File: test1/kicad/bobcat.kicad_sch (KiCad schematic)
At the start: 24 parts, among them U20 Bobcat

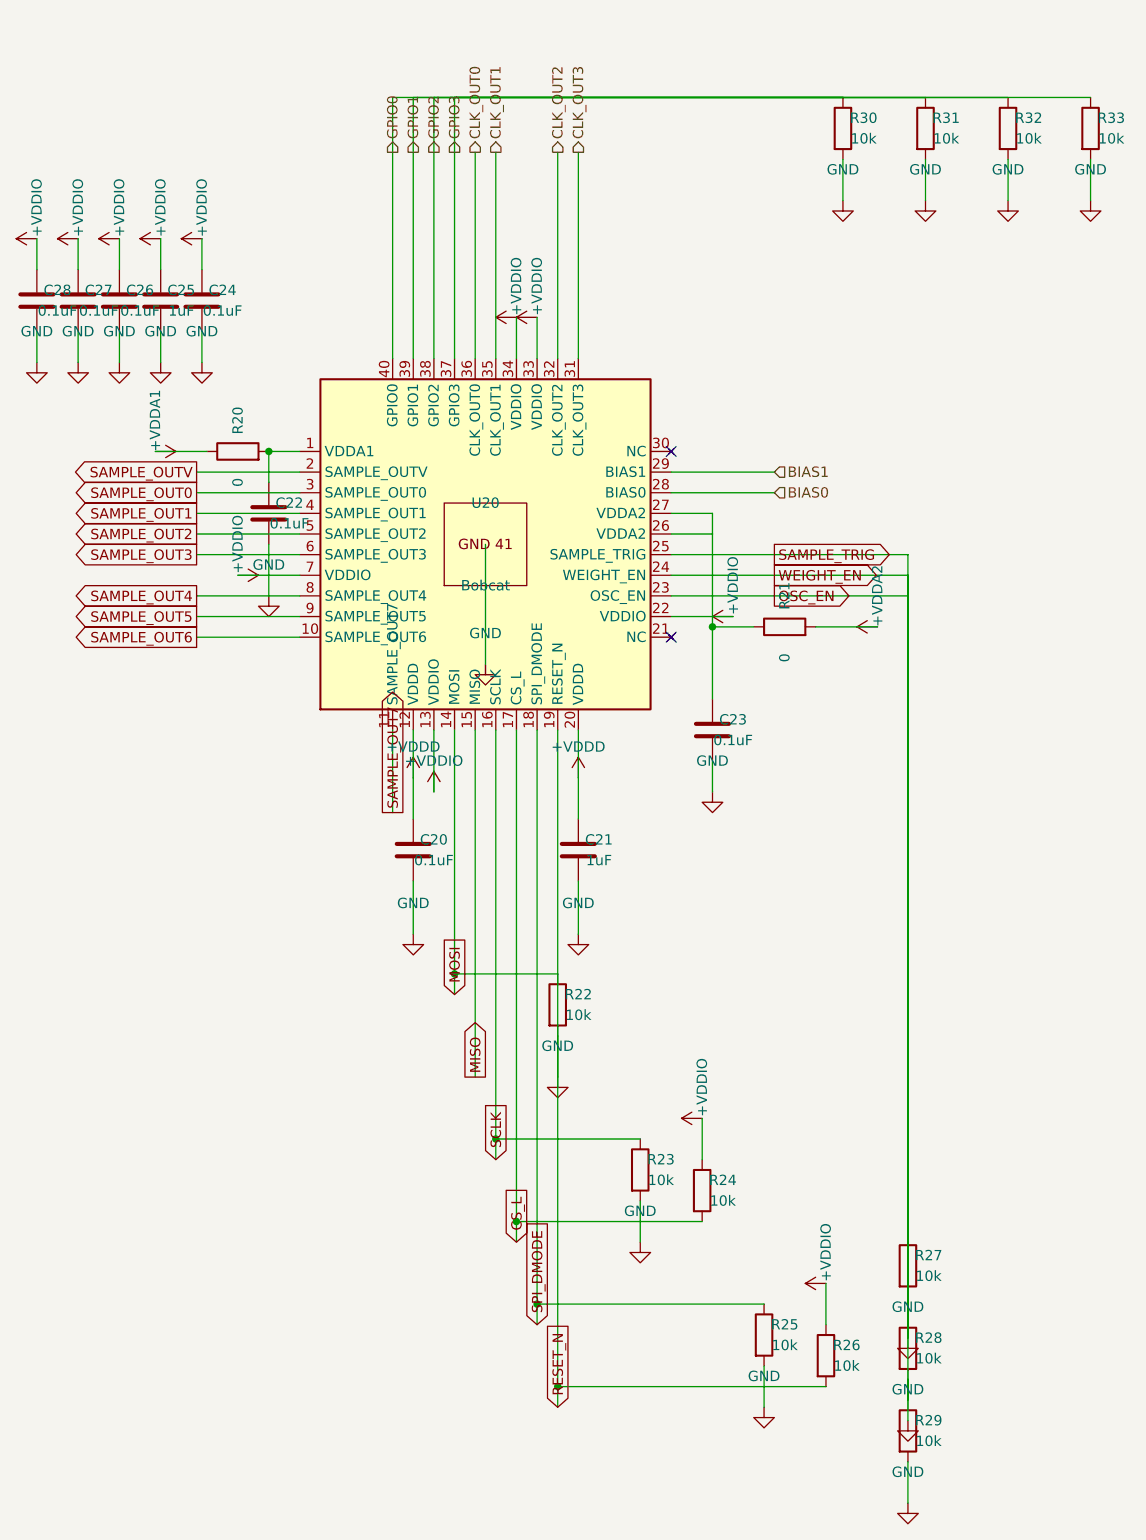
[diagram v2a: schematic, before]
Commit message: Add layout linter + cluster helpers; fix silent shorts across sheets
Introduces gen/layout_lint.py with checks for bbox spacing, wires
through/into a body, parallel-wire overlap on the same axis, bridged
drop columns, and dense GND clusters — non-fatal warnings the strict
validator cannot catch (each net's name is still present in a bridged
component's name set, so per-member name checks pass).

Fixes the bugs the linter exposed:
- FMC routing flipped to exit LEFT (pin-protrusion side) so wires no
  longer pass through the connector body
- bobcat OWT (pins 23-25) + GPIO (37-40) get one drop column per pin,
  ending the silent shorts between adjacent nets
- bobcat SPI pin 14 pull-x shifted off pin 19's column
- bias Q40/Q41 source/drain wires detoured around the body so source
  no longer shorts to drain through the same vertical
- power LDO redundant tap stubs + GND-rail dupes removed; C12 moved
  off R10's column so NR_SS doesn't short to GND
- C11 ↔ R10, J54-56 ↔ R50-52 spacing widened to meet bbox rule

Adds gnd_bus() and decoupling_cluster() helpers in gen/shared.py and
applies gnd_bus() to the eeprom address-strap pins.

Skill doc gets rules for pin-protrusion side, per-pin drop columns,
and same-axis wire overlap. All 7 sheets now pass kicad-cli parse,
the strict connectivity validator, and the layout linter.

Co-Authored-By: Claude Opus 4.7 (1M context) <noreply@anthropic.com>
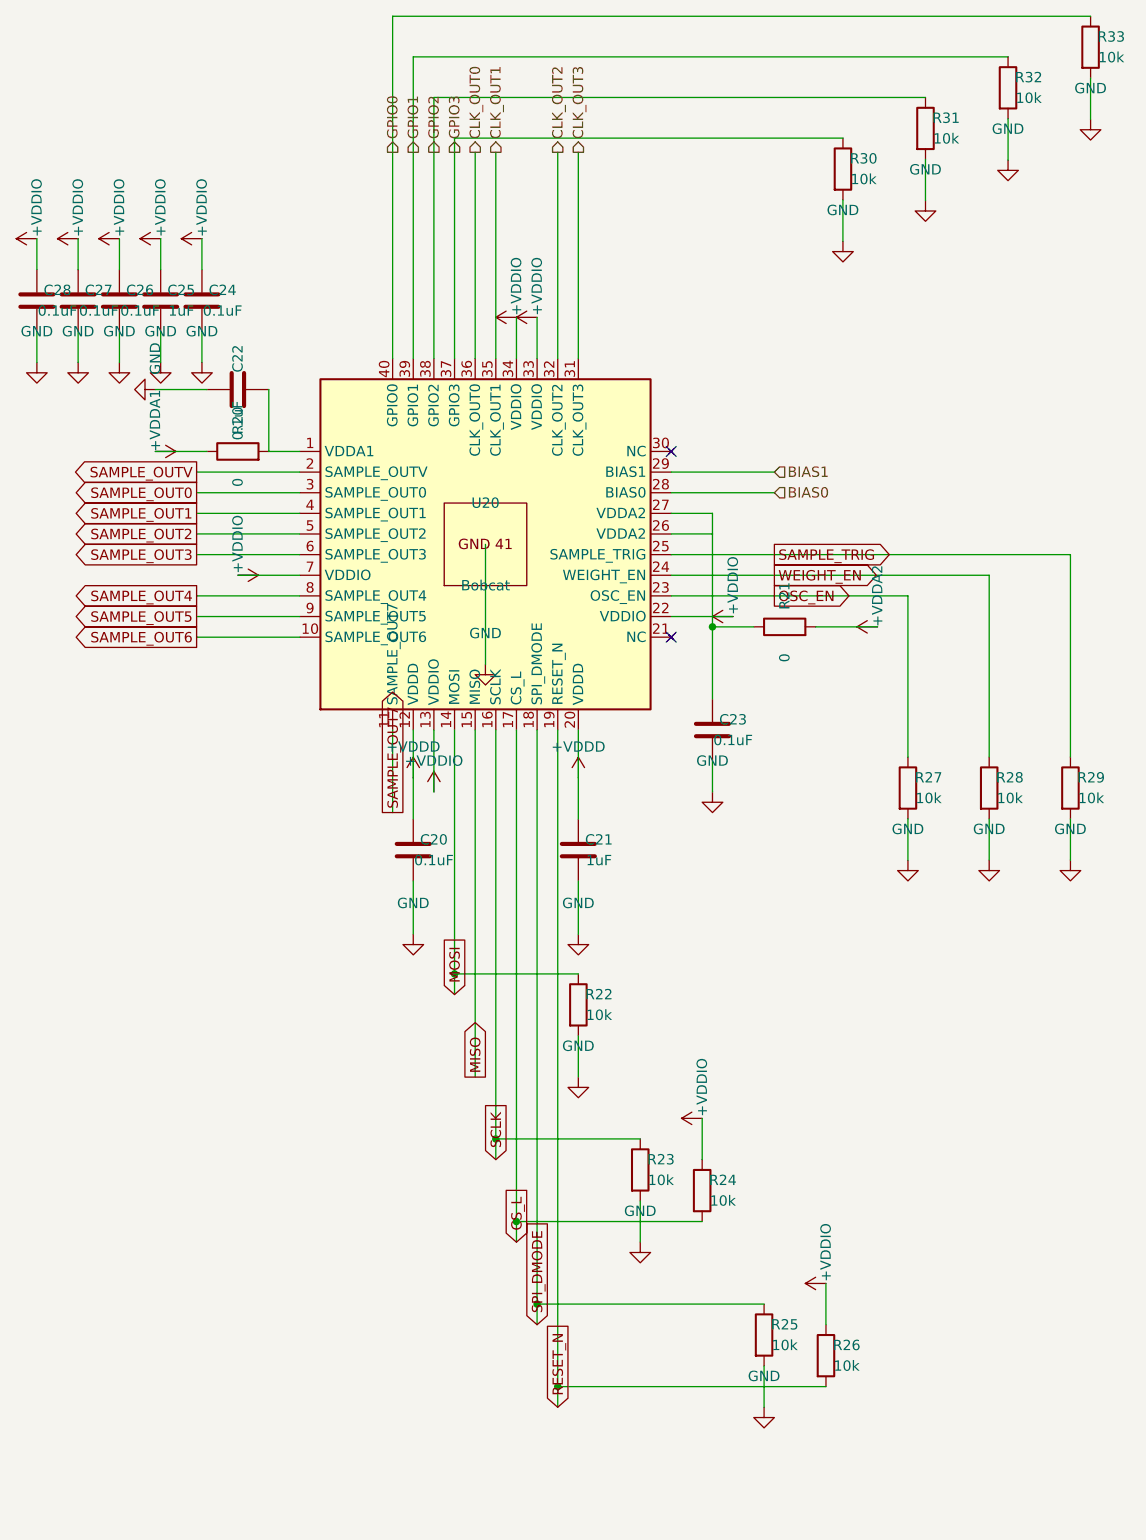
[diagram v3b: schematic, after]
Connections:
- net GND: now also C22.1; no longer C22.2, R26.2, R27.1, R28.1, R29.1, U20.19 (RESET_N), U20.23 (OSC_EN), U20.24 (WEIGHT_EN), U20.25 (SAMPLE_TRIG)
- net GPIO0: no longer R30.1, R31.1, R32.1, U20.37 (GPIO3), U20.38 (GPIO2), U20.39 (GPIO1)
- net at R20.2, U20.1 (VDDA1): now also C22.2; no longer C22.1
- new net GPIO1: R32.1, U20.39 (GPIO1)
- new net GPIO2: R31.1, U20.38 (GPIO2)
- new net GPIO3: R30.1, U20.37 (GPIO3)
- new net OSC_EN: R27.1, U20.23 (OSC_EN)
- new net RESET_N: R26.2, U20.19 (RESET_N)
- new net SAMPLE_TRIG: R29.1, U20.25 (SAMPLE_TRIG)
- new net WEIGHT_EN: R28.1, U20.24 (WEIGHT_EN)
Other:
- moved on the sheet: C22, R22, R27, R28, R29, R30, R32, R33
